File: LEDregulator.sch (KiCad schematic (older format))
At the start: 43 parts, among them J1 2.1mm DC jack, J2 2way Screw Terminal, J3 2way Screw Terminal, J4 2way Screw Terminal, J5 2way Screw Terminal, J6 2way Screw Terminal, J7 2way Screw Terminal, Q1 BSS138W, SW1 DPDT Switch, SW2 6pos rotary

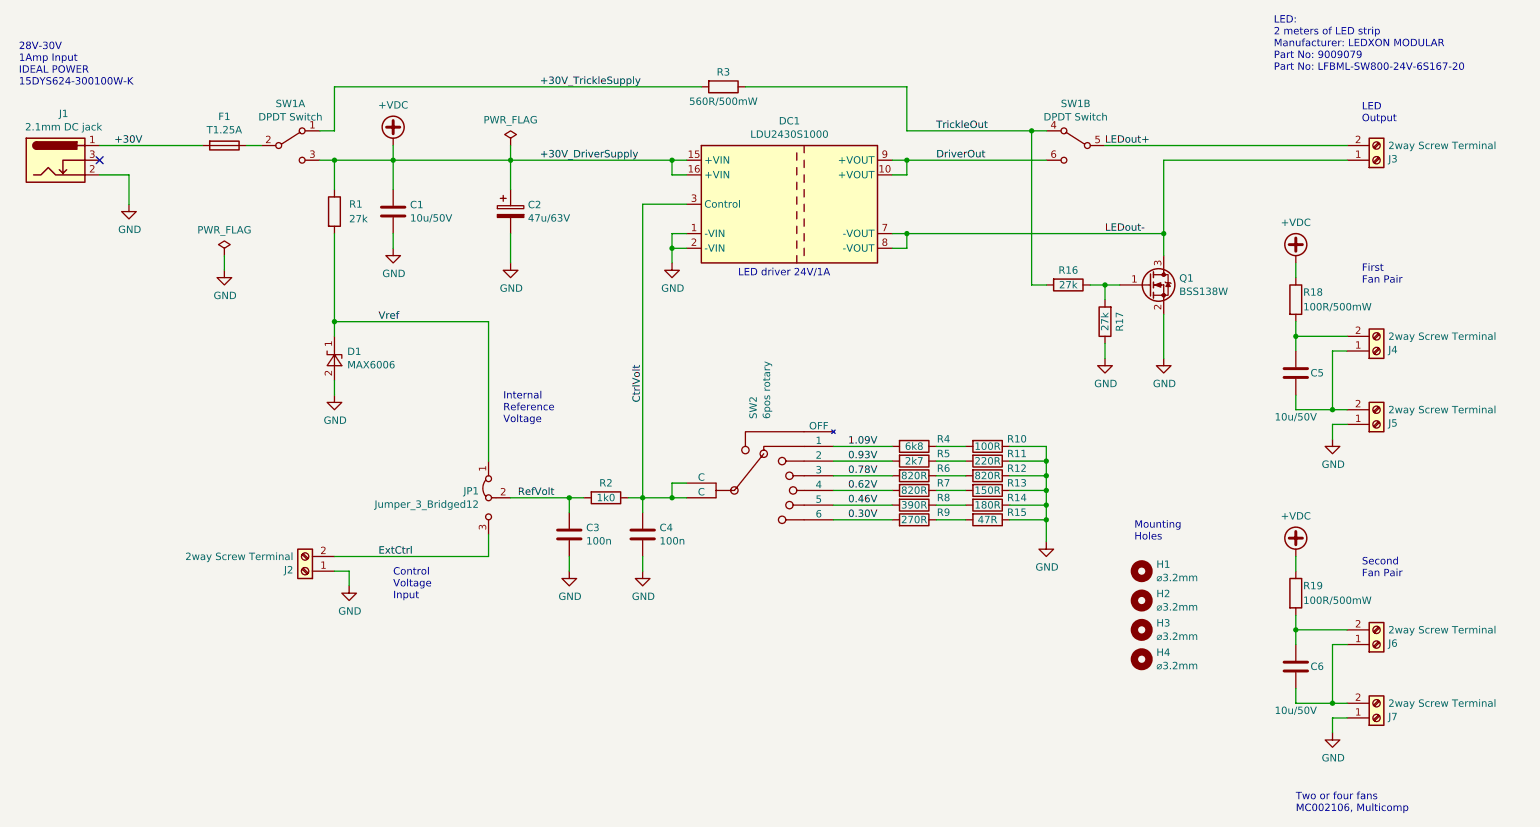
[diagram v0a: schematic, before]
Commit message: Added parts list Excell file and tidies up the schematics a bit
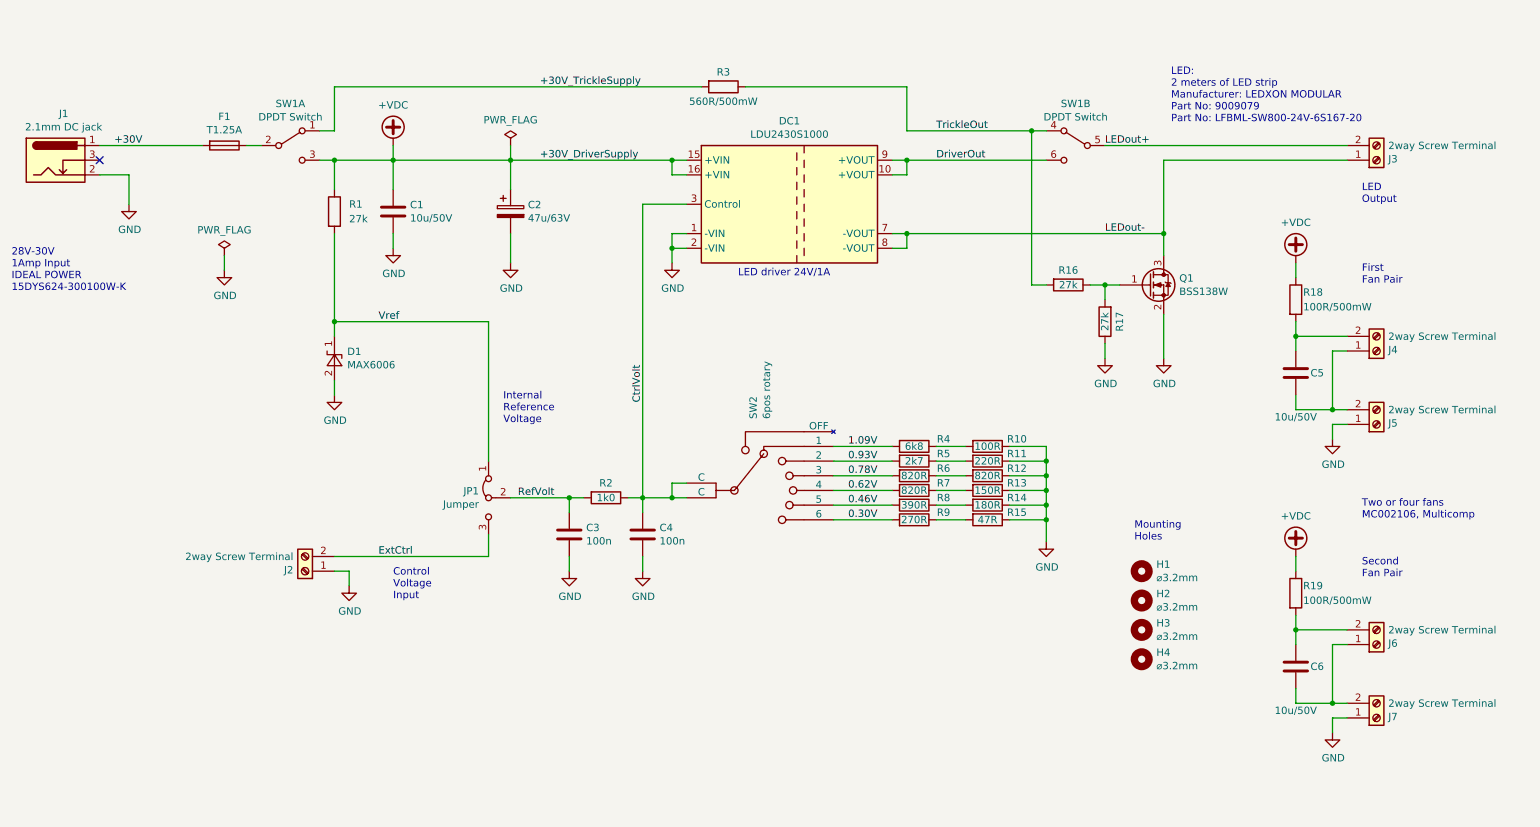
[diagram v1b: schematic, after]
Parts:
- JP1: value Jumper_3_Bridged12 -> Jumper
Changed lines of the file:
@@
 P 4150 3900
 F 0 "JP1" V 4104 3966 50  0000 L CNN
-F 1 "Jumper_3_Bridged12" V 4195 3966 50  0000 L CNN
+F 1 "Jumper" V 4195 3966 50  0000 L CNN
 F 2 "Pin_Headers:Pin_Header_Straight_1x03_Pitch2.54mm" H 4150 3900 50  0001 C CNN
 F 3 "~" H 4150 3900 50  0001 C CNN
@@
 Text Label 7200 1600 0    50   ~ 0
 DriverOut
-Text Notes 10100 1350 0    50   ~ 0
+Text Notes 10100 1900 0    50   ~ 0
 LED\nOutput
-Text Notes 950  1100 0    50   ~ 0
+Text Notes 900  2500 0    50   ~ 0
 28V-30V\n1Amp Input\nIDEAL POWER \n15DYS624-300100W-K
 $Comp
@@
 Wire Wire Line
 	2350 2350 2350 2250
-Text Notes 9650 6050 0    50   ~ 0
+Text Notes 10100 4050 0    50   ~ 0
 Two or four fans\nMC002106, Multicomp
-Text Notes 9500 1000 0    50   ~ 0
+Text Notes 8800 1350 0    50   ~ 0
 LED:\n2 meters of LED strip\nManufacturer: LEDXON MODULAR \nPart No: 9009079 \nPart No: LFBML-SW800-24V-6S167-20
 $EndSCHEMATC
